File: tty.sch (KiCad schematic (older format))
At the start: 9 parts, among them J4 ACST CPLR, Q2 BC847, U5 TLV6001DCK

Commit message: Moving and shaking, with a weird extra via
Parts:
- removed RV1: R_POT_TRIM, Potentiometer_SMD:Potentiometer_Bourns_3214W_Vertical, symbol Device:R_POT_TRIM
- added R? (x2): 50k, Resistors_SMD:R_0603_HandSoldering, symbol Device:R
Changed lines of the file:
@@
 L power:VEE #PWR?
 U 1 1 5ED3C47C
-P 5700 4000
+P 5800 4000
 AR Path="/5ED3C47C" Ref="#PWR?"  Part="1"
 AR Path="/5ED35417/5ED3C47C" Ref="#PWR0108"  Part="1"
-F 0 "#PWR0108" H 5700 3850 50  0001 C CNN
-F 1 "VEE" H 5717 4173 50  0000 C CNN
-F 2 "" H 5700 4000 50  0001 C CNN
-F 3 "" H 5700 4000 50  0001 C CNN
-	1    5700 4000
+F 0 "#PWR0108" H 5800 3850 50  0001 C CNN
+F 1 "VEE" H 5817 4173 50  0000 C CNN
+F 2 "" H 5800 4000 50  0001 C CNN
+F 3 "" H 5800 4000 50  0001 C CNN
+	1    5800 4000
 	1    0    0    -1
 $EndComp
@@
 $EndComp
 Wire Wire Line
-	5700 4000 5700 4100
+	5800 4000 5800 4100
 Wire Wire Line
 	5350 2900 5450 2900
@@
 	1    0    0    -1
 $EndComp
-$Comp
-L Device:R_POT_TRIM RV?
-U 1 1 5ED3C4B3
-P 5450 4100
-AR Path="/5ED3C4B3" Ref="RV?"  Part="1"
-AR Path="/5ED35417/5ED3C4B3" Ref="RV1"  Part="1"
-F 0 "RV1" V 5335 4100 50  0000 C CNN
-F 1 "R_POT_TRIM" V 5244 4100 50  0000 C CNN
-F 2 "Potentiometer_SMD:Potentiometer_Bourns_3214W_Vertical" H 5450 4100 50  0001 C CNN
-F 3 "~" H 5450 4100 50  0001 C CNN
-	1    5450 4100
-	0    1    -1   0
-$EndComp
 Wire Wire Line
 	4600 4100 4450 4100
@@
 	4600 4100 4600 3500
 Connection ~ 4600 4100
-Wire Wire Line
-	4600 4100 5300 4100
-Wire Wire Line
-	5600 4100 5700 4100
-Wire Wire Line
-	5450 3950 5450 3600
 $Comp
 L Connector_Generic:Conn_02x03_Odd_Even J?
@@
 -VDC
 Wire Wire Line
-	5700 4100 5700 4400
-Wire Wire Line
 	5700 4400 4450 4400
-Connection ~ 5700 4100
 Text HLabel 4450 4400 0    50   Input ~ 0
 Vee
+Wire Wire Line
+	5050 4100 4600 4100
+$Comp
+L Device:R R?
+U 1 1 5DE8C764
+P 5650 4100
+AR Path="/5DE8C764" Ref="R?"  Part="1"
+AR Path="/5ED35417/5DE8C764" Ref="R?"  Part="1"
+F 0 "R?" V 5765 4100 50  0000 C CNN
+F 1 "50k" V 5650 4100 50  0000 C CNN
+F 2 "Resistors_SMD:R_0603_HandSoldering" V 5580 4100 50  0001 C CNN
+F 3 "~" H 5650 4100 50  0001 C CNN
+	1    5650 4100
+	0    1    1    0
+$EndComp
+$Comp
+L Device:R R?
+U 1 1 5DE8C76A
+P 5200 4100
+AR Path="/5DE8C76A" Ref="R?"  Part="1"
+AR Path="/5ED35417/5DE8C76A" Ref="R?"  Part="1"
+F 0 "R?" V 5300 4100 50  0000 C CNN
+F 1 "50k" V 5200 4100 50  0000 C CNN
+F 2 "Resistors_SMD:R_0603_HandSoldering" V 5130 4100 50  0001 C CNN
+F 3 "~" H 5200 4100 50  0001 C CNN
+	1    5200 4100
+	0    1    1    0
+$EndComp
+Wire Wire Line
+	5350 4100 5450 4100
+Wire Wire Line
+	5450 3600 5450 4100
+Connection ~ 5450 4100
+Wire Wire Line
+	5450 4100 5500 4100
 $EndSCHEMATC

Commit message: Tweaks, reconnect Vee
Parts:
- gave numbers to parts that had none: 2
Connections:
- wire segments 30 -> 31
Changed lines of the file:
@@
 Text HLabel 6950 3750 2    50   Output ~ 0
 -VDC
-Wire Wire Line
-	5700 4400 4450 4400
 Text HLabel 4450 4400 0    50   Input ~ 0
 Vee
@@
 P 5650 4100
 AR Path="/5DE8C764" Ref="R?"  Part="1"
-AR Path="/5ED35417/5DE8C764" Ref="R?"  Part="1"
-F 0 "R?" V 5765 4100 50  0000 C CNN
+AR Path="/5ED35417/5DE8C764" Ref="R9"  Part="1"
+F 0 "R9" V 5765 4100 50  0000 C CNN
 F 1 "50k" V 5650 4100 50  0000 C CNN
 F 2 "Resistors_SMD:R_0603_HandSoldering" V 5580 4100 50  0001 C CNN
@@
 P 5200 4100
 AR Path="/5DE8C76A" Ref="R?"  Part="1"
-AR Path="/5ED35417/5DE8C76A" Ref="R?"  Part="1"
-F 0 "R?" V 5300 4100 50  0000 C CNN
+AR Path="/5ED35417/5DE8C76A" Ref="R8"  Part="1"
+F 0 "R8" V 5300 4100 50  0000 C CNN
 F 1 "50k" V 5200 4100 50  0000 C CNN
 F 2 "Resistors_SMD:R_0603_HandSoldering" V 5130 4100 50  0001 C CNN
@@
 Wire Wire Line
 	5450 4100 5500 4100
+Wire Wire Line
+	5800 4400 5800 4100
+Wire Wire Line
+	4450 4400 5800 4400
+Connection ~ 5800 4100
 $EndSCHEMATC

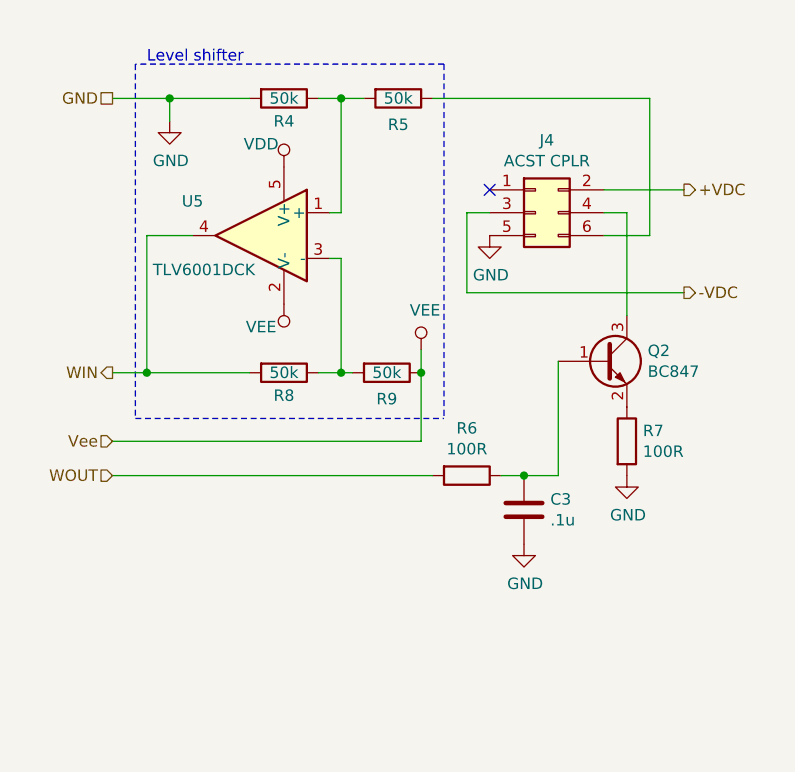
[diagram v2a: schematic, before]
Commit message: Use MAX3180 for incoming RS-232
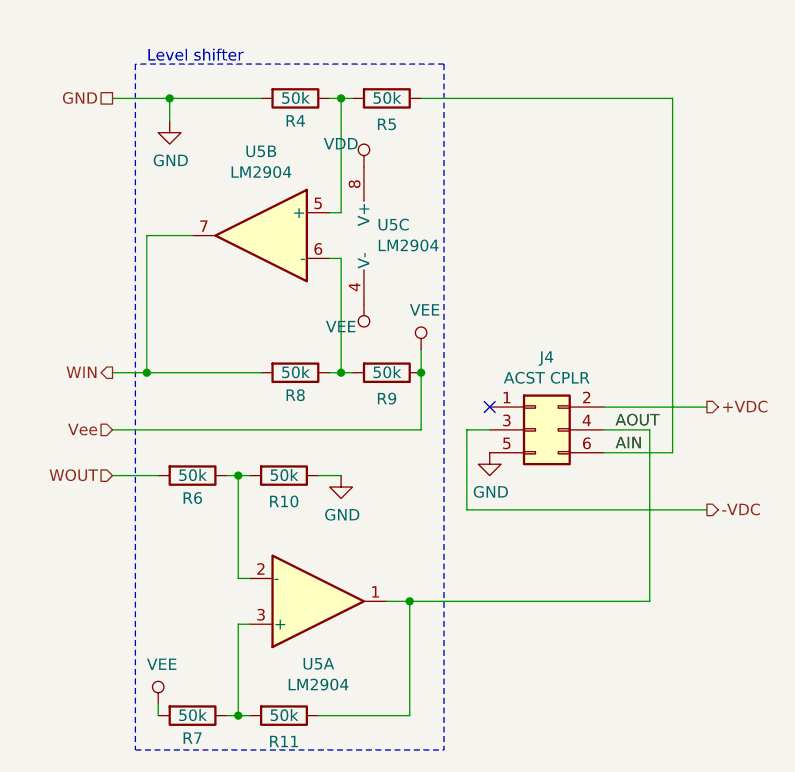
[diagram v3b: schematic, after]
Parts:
- removed C3: .1u, Capacitor_SMD:C_0603_1608Metric_Pad1.05x0.95mm_HandSolder, symbol Device:C
- removed Q2: BC847, Package_TO_SOT_SMD:SOT-23, symbol Transistor_BJT:BC847
- removed U5: TLV6001DCK, Package_TO_SOT_SMD:SOT-353_SC-70-5, symbol Amplifier_Operational:TLV6001DCK
- added R10, R11: 50k, Resistors_SMD:R_0603_HandSoldering, symbol Device:R
- added U5: LM2904, Package_SO:VSSOP-8_3.0x3.0mm_P0.65mm, symbol Amplifier_Operational:LM2904
- R6, R7: value 100R -> 50k
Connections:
- net GND: now also R10.1; no longer R7.2
- net VDD: now also U5.8 (V+)
- net VEE: now also R7.2, U5.4 (V-)
- net WIN: now also U5.7
- net at R8.1, R9.2: now also U5.6 (-)
- net AIN: now reaches J4.6 (Pin_6), R5.1
- net at R4.1, R5.2: now also U5.5 (+)
- net at R7.1: now also R11.2, U5.3 (+)
- net at R6.1: now also R10.2, U5.2 (-)
- net AOUT: now reaches J4.4 (Pin_4)
- net AOUT: now also R11.1, U5.1
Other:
- moved on the sheet: J4, R4, R5, R8

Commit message: Get rid of hand-soldering footprints in schematic too
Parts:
- R10, R11, R4, R5, R6, R7, R8, R9: footprint Resistors_SMD:R_0603_HandSoldering -> Resistors_SMD:R_0603
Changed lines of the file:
@@
 F 0 "R5" V 5765 2900 50  0000 C CNN
 F 1 "50k" V 5650 2900 50  0000 C CNN
-F 2 "Resistors_SMD:R_0603_HandSoldering" V 5580 2900 50  0001 C CNN
+F 2 "Resistors_SMD:R_0603" V 5580 2900 50  0001 C CNN
 F 3 "~" H 5650 2900 50  0001 C CNN
 	1    5650 2900
@@
 F 0 "R4" V 5350 2900 50  0000 C CNN
 F 1 "50k" V 5250 2900 50  0000 C CNN
-F 2 "Resistors_SMD:R_0603_HandSoldering" V 5180 2900 50  0001 C CNN
+F 2 "Resistors_SMD:R_0603" V 5180 2900 50  0001 C CNN
 F 3 "~" H 5250 2900 50  0001 C CNN
 	1    5250 2900
@@
 F 0 "R9" V 5765 4100 50  0000 C CNN
 F 1 "50k" V 5650 4100 50  0000 C CNN
-F 2 "Resistors_SMD:R_0603_HandSoldering" V 5580 4100 50  0001 C CNN
+F 2 "Resistors_SMD:R_0603" V 5580 4100 50  0001 C CNN
 F 3 "~" H 5650 4100 50  0001 C CNN
 	1    5650 4100
@@
 F 0 "R8" V 5350 4100 50  0000 C CNN
 F 1 "50k" V 5250 4100 50  0000 C CNN
-F 2 "Resistors_SMD:R_0603_HandSoldering" V 5180 4100 50  0001 C CNN
+F 2 "Resistors_SMD:R_0603" V 5180 4100 50  0001 C CNN
 F 3 "~" H 5250 4100 50  0001 C CNN
 	1    5250 4100
@@
 F 0 "R6" V 4900 4550 50  0000 C CNN
 F 1 "50k" V 4800 4550 50  0000 C CNN
-F 2 "Resistors_SMD:R_0603_HandSoldering" V 4730 4550 50  0001 C CNN
+F 2 "Resistors_SMD:R_0603" V 4730 4550 50  0001 C CNN
 F 3 "~" H 4800 4550 50  0001 C CNN
 	1    4800 4550
@@
 F 0 "R10" V 5315 4550 50  0000 C CNN
 F 1 "50k" V 5200 4550 50  0000 C CNN
-F 2 "Resistors_SMD:R_0603_HandSoldering" V 5130 4550 50  0001 C CNN
+F 2 "Resistors_SMD:R_0603" V 5130 4550 50  0001 C CNN
 F 3 "~" H 5200 4550 50  0001 C CNN
 	1    5200 4550
@@
 F 0 "R7" V 4900 5600 50  0000 C CNN
 F 1 "50k" V 4800 5600 50  0000 C CNN
-F 2 "Resistors_SMD:R_0603_HandSoldering" V 4730 5600 50  0001 C CNN
+F 2 "Resistors_SMD:R_0603" V 4730 5600 50  0001 C CNN
 F 3 "~" H 4800 5600 50  0001 C CNN
 	1    4800 5600
@@
 F 0 "R11" V 5315 5600 50  0000 C CNN
 F 1 "50k" V 5200 5600 50  0000 C CNN
-F 2 "Resistors_SMD:R_0603_HandSoldering" V 5130 5600 50  0001 C CNN
+F 2 "Resistors_SMD:R_0603" V 5130 5600 50  0001 C CNN
 F 3 "~" H 5200 5600 50  0001 C CNN
 	1    5200 5600

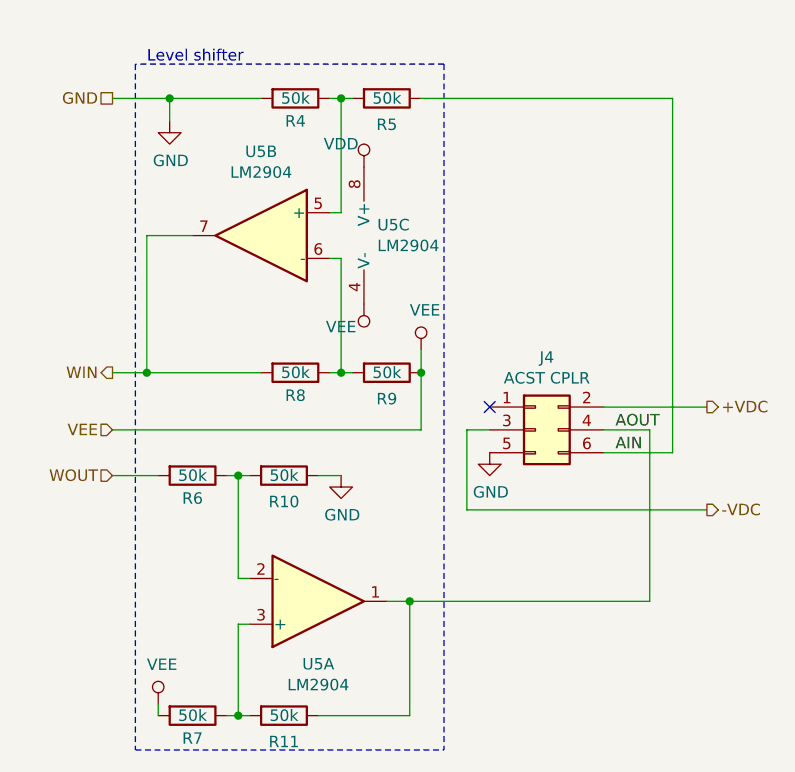
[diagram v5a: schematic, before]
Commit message: Adjust tty schematic cosmetically
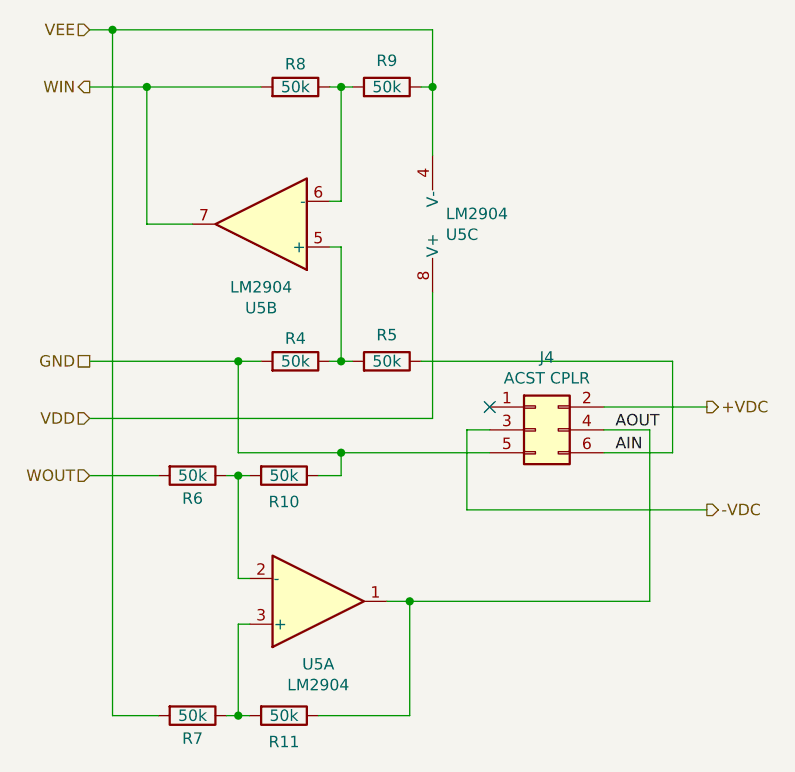
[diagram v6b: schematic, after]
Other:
- note removed: "Level shifter"
- moved on the sheet: R4, R5, R8, R9, U5B, U5C
